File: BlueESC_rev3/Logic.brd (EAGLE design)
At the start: 24.4 x 36 mm, 83 parts, among them Q1 BC817-40W, Q2 BC817-40W, Q3 BC817-40W, Q4 SI7370, Q5 SI7370, Q6 SI7370, Q7 SI7370, Q8 SI7370, Q9 SI7370, U1 ATMEGA168, U2 V_REG_LDOSMD, Y1 RESONATORSMD

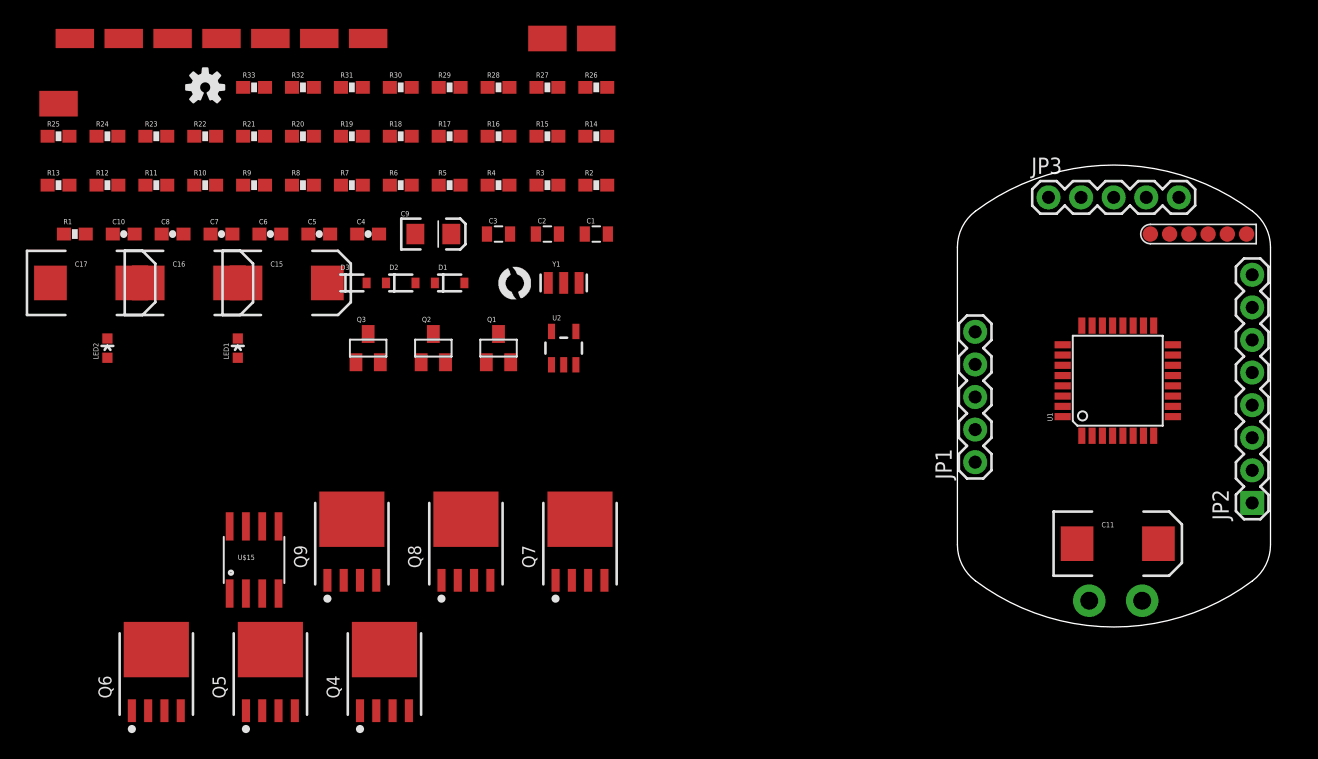
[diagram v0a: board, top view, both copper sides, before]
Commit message: Rev3 (two boards) laid out and ready to go. Final review may create a few changes.
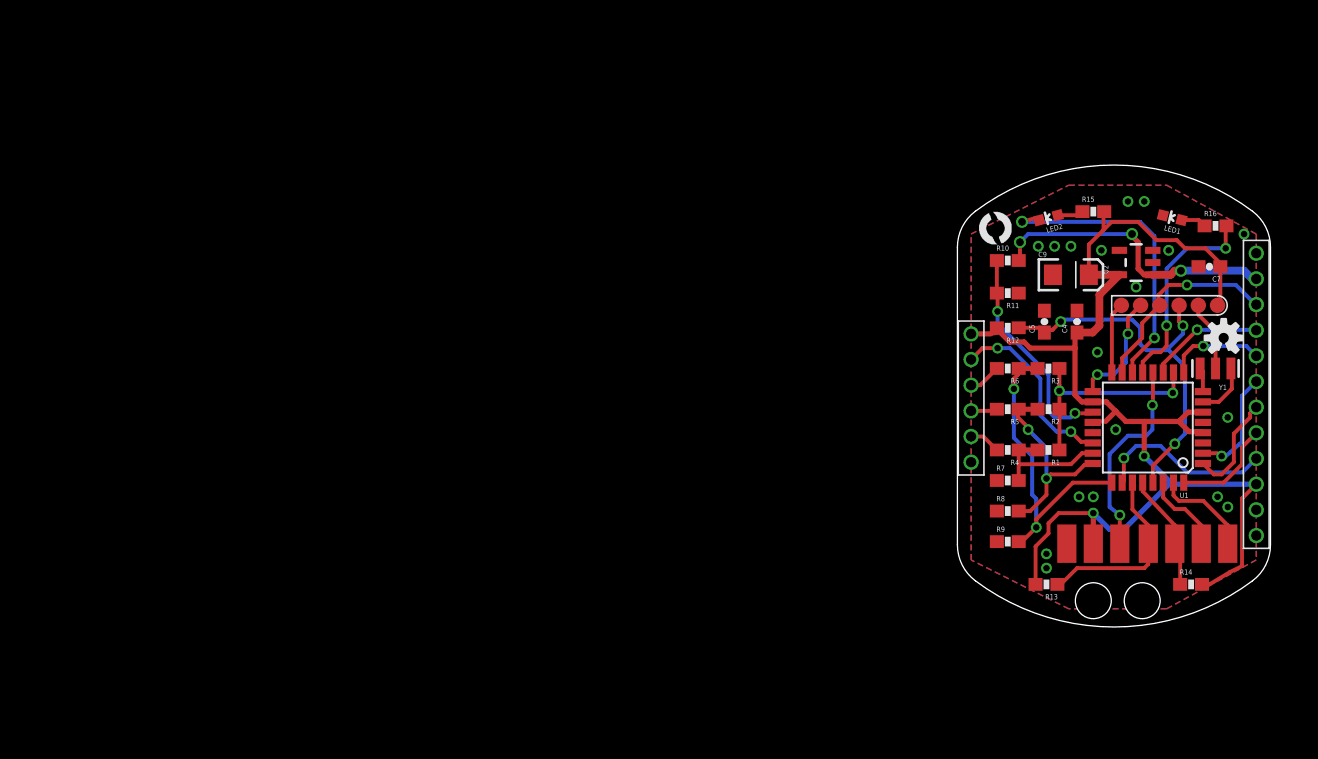
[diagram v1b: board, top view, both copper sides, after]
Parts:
- removed C1, C2, C3: 1uF, SparkFun-Capacitors:0805
- removed C10, C6, C8: 0.1uF, SparkFun-Capacitors:0603-CAP
- removed C11, C15, C16, C17: 47uF, SparkFun-Capacitors:EIA7343
- removed D1, D2, D3: Schottky, SparkFun-DiscreteSemi:SOD-323
- removed JP1, JP3: (no value), SparkFun-Connectors:1X05
- removed JP2: (no value), SparkFun-Connectors:1X08
- removed Q1, Q2, Q3: BC817-40W, SparkFun-DiscreteSemi:SOT23
- removed Q4, Q5, Q6, Q7, Q8, Q9: SI7370, transistor-fet-bobstarr:POWERPAK-SO-08
- removed R17, R23, R28: 2.2K, SparkFun-Resistors:0603-RES
- removed R18, R24, R29: 4.7K, SparkFun-Resistors:0603-RES
- removed R19, R21, R25, R26, R30, R31: 100, SparkFun-Resistors:0603-RES
- removed R20: 3.3K, SparkFun-Resistors:0603-RES
- removed R22, R27, R32, R33: 10K, SparkFun-Resistors:0603-RES
- removed U$1, U$2: PADPTH-MED, BR-Eagle-Library:PAD-PTH-MED-1
- removed U$15: ACS712, SparkFun-AnalogIC:SO08
- removed U$5, U$6, U$7: PAD2X3MM, BR-Eagle-Library:PAD-2X3MM
- added U$16: HEADER-62MM, BR-Eagle-Library:HEADER-2MM-6POS
- added U$17: HEADER-122MM, BR-Eagle-Library:HEADER-2MM-12POS
- LED1: value Yellow -> RED
- LED2: value Green -> BLUE
- moved U$13 98.1 mm to (34.0, 15.2), turned to 90 degrees
- moved U$12 92.7 mm to (31.9, 15.2), turned to 90 degrees
- moved U$10 84.1 mm to (29.8, 15.2), turned to 90 degrees
- moved U$11 83.7 mm to (25.6, 15.2), turned to 90 degrees
- moved R13 83.0 mm to (19.8, 12.1), turned to 180 degrees
- moved LOGO1 81.7 mm to (33.7, 31.3)
- moved U$9 78.9 mm to (27.8, 15.2), turned to 90 degrees
- moved R1 77.7 mm to (20.0, 22.5), turned to 180 degrees
- moved C7 77.0 mm to (32.5, 36.8), turned to 180 degrees
- moved LED2 74.0 mm to (20.0, 40.6), turned to 105 degrees
- moved LED1 73.5 mm to (29.6, 40.6), turned to 76 degrees
- moved U$8 72.0 mm to (23.5, 15.2), turned to 90 degrees
- moved R12 71.0 mm to (16.8, 32.1), turned to 180 degrees
- moved U$3 67.2 mm to (21.4, 15.2), turned to 90 degrees
- moved R11 66.9 mm to (16.8, 34.8), turned to 180 degrees
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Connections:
- removed net GATE_AH: Q4.4, R19.2
- removed net GATE_AL: Q5.4, R21.2, R22.2
- removed net GATE_BH: Q6.4, R25.2
- removed net GATE_BL: Q7.4, R26.2, R27.2
- removed net GATE_CH: Q8.4, R30.2
- removed net GATE_CL: Q9.4, R31.2, R32.2
- removed net N$1: C8.1, U$15.6
- removed net N$12: C3.1, D1.C, R17.2
- removed net N$15: C1.1, D2.C, R23.2
- removed net N$19: C2.1, D3.C, R28.2
- removed net N$2: Q1.1, R18.2
- removed net N$4: Q1.3, R17.1, R19.1
- removed net N$5: Q2.1, R24.2
- removed net N$6: Q2.3, R23.1, R25.1
- removed net N$7: Q3.1, R29.2
- removed net N$8: C6.1, U1.20
- removed net N$9: Q3.3, R28.1, R30.1
- removed net VBAT+: U$1.P$1, U$15.1, U$15.2
- net CURRENT_ADC: now also U$17.P$4, U1.26; no longer JP3.2, U$15.7, U1.19
- net GND: now also U$16.P$1, U$17.P$1, U$17.P$12, U$17.P$2; no longer C10.2, C11.C, C15.C, C16.C, C17.C, C6.2, C8.2, JP1.1, JP1.5, JP2.1, JP2.8, JP3.5, Q1.2, Q2.2, Q3.2, Q5.3, Q7.3, Q9.3, R22.1, R27.1, R32.1, R33.1, U$15.5, U$2.P$1
- net LED_STATUS: now also U1.14; no longer U1.11
- net LED_WARN: now also U1.13; no longer U1.32
- net PHASE_A: now also U$16.P$2; no longer C3.2, JP1.2, Q4.3, Q5.5-8, U$5.P$1
- net PHASE_B: now also U$16.P$3; no longer C1.2, JP1.3, Q6.3, Q7.5-8, U$6.P$1
- net PHASE_C: now also U$16.P$4; no longer C2.2, JP1.4, Q8.3, Q9.5-8, U$7.P$1
- net PWM_AH: now also U$17.P$5, U1.32; no longer JP2.2, R18.1, U$14.MOSI, U1.15
- net PWM_AL: now also U$17.P$6; no longer JP2.3, R21.1
- net PWM_BH: now also U$17.P$7, U1.2; no longer JP2.4, R24.1, U1.14
- net PWM_BL: now also U$17.P$8, U1.9; no longer JP2.5, R26.1, U1.2
- net PWM_CH: now also U$17.P$9, U1.11; no longer JP2.6, R29.1, U1.13
- net PWM_CL: now also U$14.MOSI, U$17.P$10, U1.15; no longer JP2.7, R31.1, U1.9
- net TEMP_ADC: now also U$16.P$5, U1.22; no longer JP3.1, R20.1, R33.2, U1.26
- net VBAT: now also U$17.P$11; no longer C11.A, C15.A, C16.A, C17.A, D1.A, D2.A, D3.A, JP3.3, Q4.5-8, Q6.5-8, Q8.5-8, U$15.3, U$15.4, U2.3
- net VBAT_ADC: now also U1.19; no longer U1.22
- net VCC5V: now also U$16.P$6, U$17.P$3, U1.20; no longer C10.1, JP3.4, R20.2, U$15.8
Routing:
- net VCC5V: track 0.00 -> 100.2 mm, vias 0 -> 2
- net RESET: track 0.00 -> 30.0 mm, vias 0 -> 3
- net SENSE_C: track 0.00 -> 24.3 mm, vias 0 -> 2
- net LED_STATUS: track 0.00 -> 23.6 mm, vias 0 -> 2
- net VBAT: track 0.00 -> 23.2 mm, vias 0 -> 3
- net VBAT_ADC: track 0.00 -> 17.2 mm, vias 0 -> 2
- net CENTER: track 0.00 -> 16.9 mm, vias 0 -> 2
- net LED_WARN: track 0.00 -> 16.3 mm, vias 0 -> 2
- net PWM: track 0.00 -> 16.0 mm, vias 0 -> 2
- net PWM_CL: track 0.00 -> 15.9 mm, vias 0 -> 1
- net SENSE_B: track 0.00 -> 15.8 mm, vias 0 -> 2
- net SDA: track 0.00 -> 14.6 mm
- net TEMP_ADC: track 0.00 -> 14.6 mm, vias 0 -> 2
- net CURRENT_ADC: track 0.00 -> 14.0 mm, vias 0 -> 1
- net SENSE_A: track 0.00 -> 9.98 mm
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- added copper zone on layer 1, net GND
- added copper zone on layer 16, net GND
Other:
- board text added: "+"
- board text added: "-"
- board text added: "5V"
- board text added: "9/14"
- board text added: "BLUESC-ELEC-LOGIC-XA"
- board text added: "BlueRobotics"
- board text added: "Designed by R.J."
- board text added: "GND"
- board text added: "PWM"
- board text added: "RX"
- board text added: "SCL"
- board text added: "SDA"
- board text added: "TX"

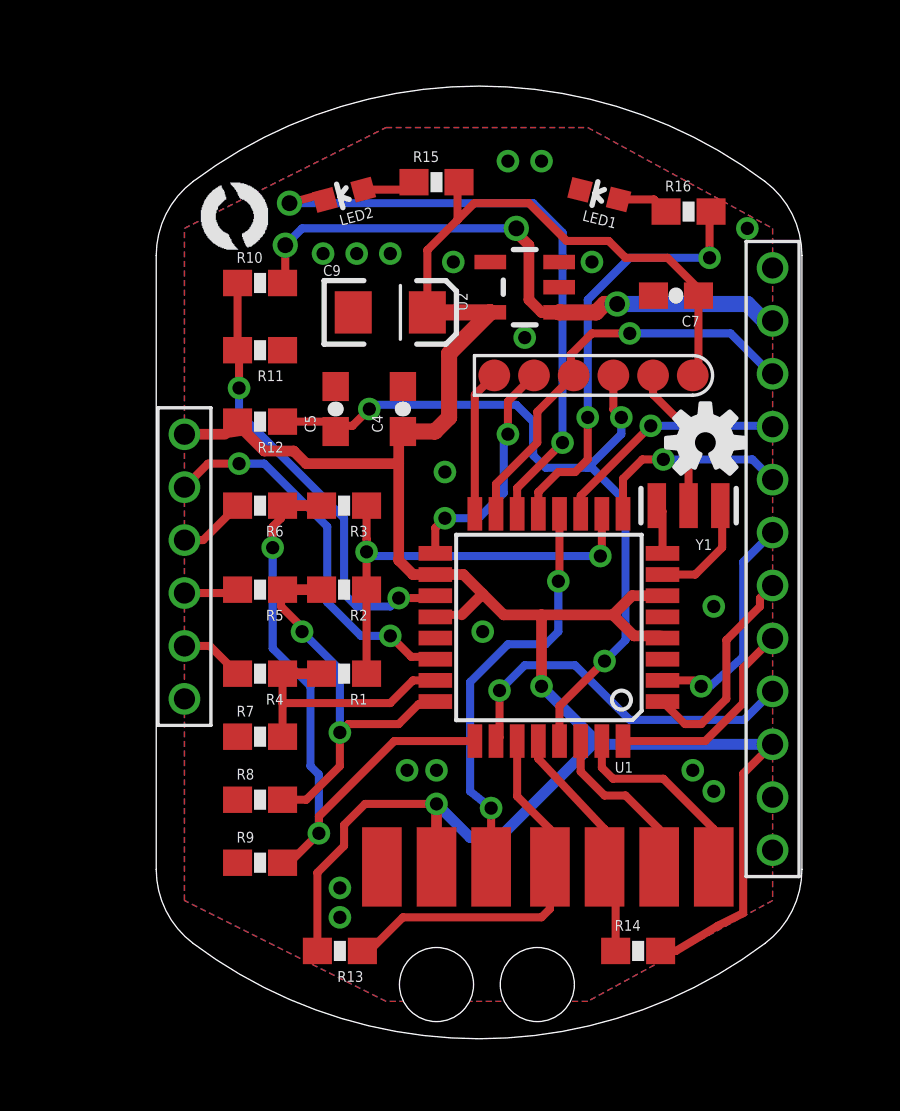
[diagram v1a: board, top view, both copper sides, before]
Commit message: Rev 3 changes. Boards have been ordered.
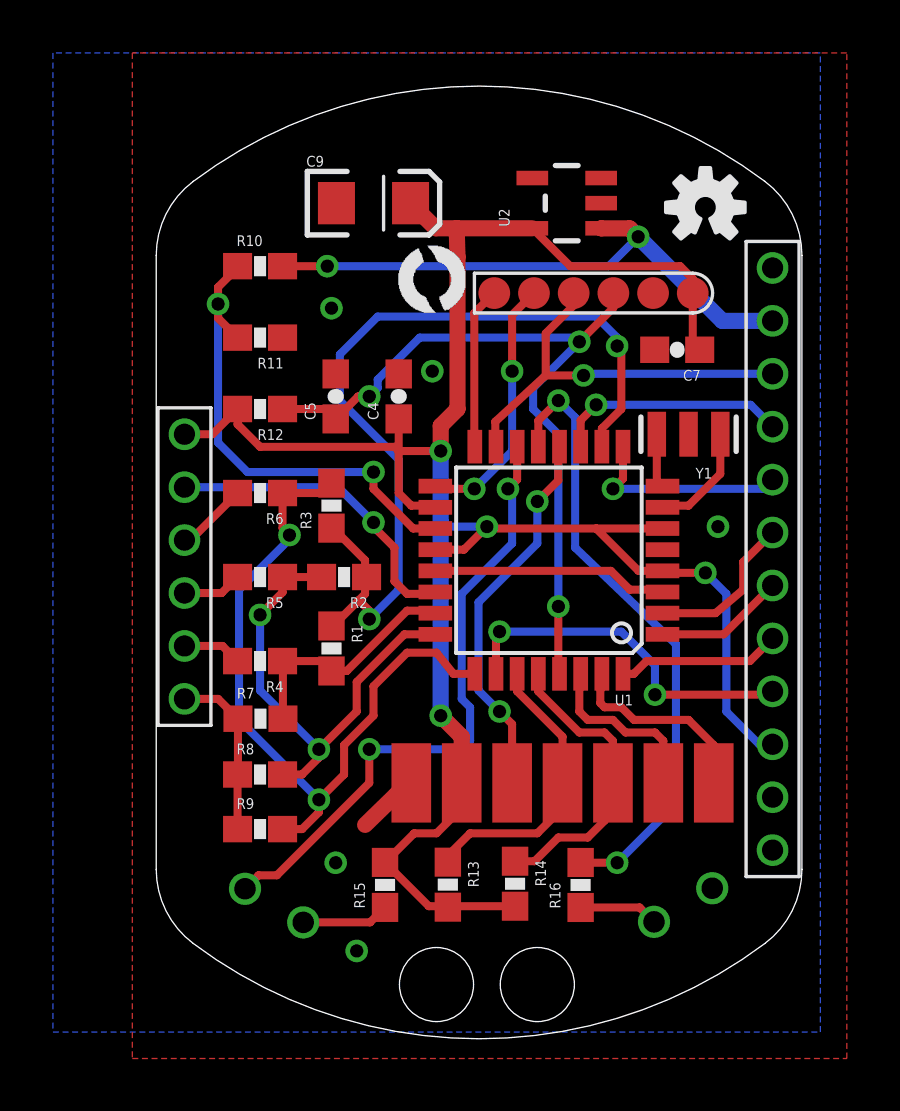
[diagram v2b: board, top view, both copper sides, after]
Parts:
- LED1, LED2: device SparkFun:LED-0603 -> SparkFun:LED3MM-NS
- R15, R16: value 330 -> 22
- moved LED1 27.0 mm to (32.8, 13.8), turned to 30 degrees
- moved LED2 27.0 mm to (17.4, 13.8), turned to 150 degrees
- moved R15 26.6 mm to (21.6, 14.6), turned to 90 degrees
- moved R16 25.8 mm to (28.9, 14.6), turned to 90 degrees
- moved LOGO1 8.89 mm to (33.7, 40.2)
- moved U$4 7.83 mm to (22.1, 36.2)
- moved R14 5.30 mm to (26.5, 14.6), turned to 270 degrees
- moved R13 4.79 mm to (23.9, 14.6), turned to 270 degrees
- moved C9 4.18 mm to (21.1, 40.3)
- moved U2 3.55 mm to (28.4, 40.3)
- moved U$3 3.36 mm to (22.5, 18.4)
- moved U$8 3.31 mm to (24.4, 18.4)
- moved U$11 3.27 mm to (26.4, 18.4)
- moved U$9 3.21 mm to (28.3, 18.4)
- moved U$10 3.19 mm to (30.2, 18.4)
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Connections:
- net GND: now also LED1.K; no longer LED1.C
- net LED_STATUS: now also LED2.K; no longer LED2.C
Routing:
- net CENTER: track 16.9 -> 33.0 mm
- net VCC5V: track 100.2 -> 85.8 mm, vias 2 -> 4
- net GND: track 5.48 -> 17.8 mm, vias 18 -> 5
- net LED_WARN: track 16.3 -> 23.7 mm
- net SENSE_C: track 24.3 -> 27.7 mm
- net SDA: track 14.6 -> 11.2 mm
- net PWM_AL: track 8.17 -> 4.92 mm
- net PWM_BH: track 8.90 -> 5.99 mm, vias 1 -> 0
- net TEMP_ADC: track 14.6 -> 12.0 mm, vias 2 -> 1
- net SCL: track 9.10 -> 11.4 mm
- net SENSE_B: track 15.8 -> 18.1 mm
- net PWM_AH: track 8.04 -> 6.21 mm
- net PWM: track 16.0 -> 14.5 mm
- net VBAT: track 23.2 -> 21.8 mm, vias 3 -> 2
- net N$16: track 2.03 -> 3.33 mm
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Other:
- board text added: "BLUESC-ELEC-LOGIC-X1A"
- board text added: "Blue"
- board text added: "BlueESC"
- board text added: "Robotics"
- board text removed: "BLUESC-ELEC-LOGIC-XA"
